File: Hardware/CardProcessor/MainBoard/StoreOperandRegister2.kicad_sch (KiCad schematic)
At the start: 2 parts, among them U43 74ABT16374

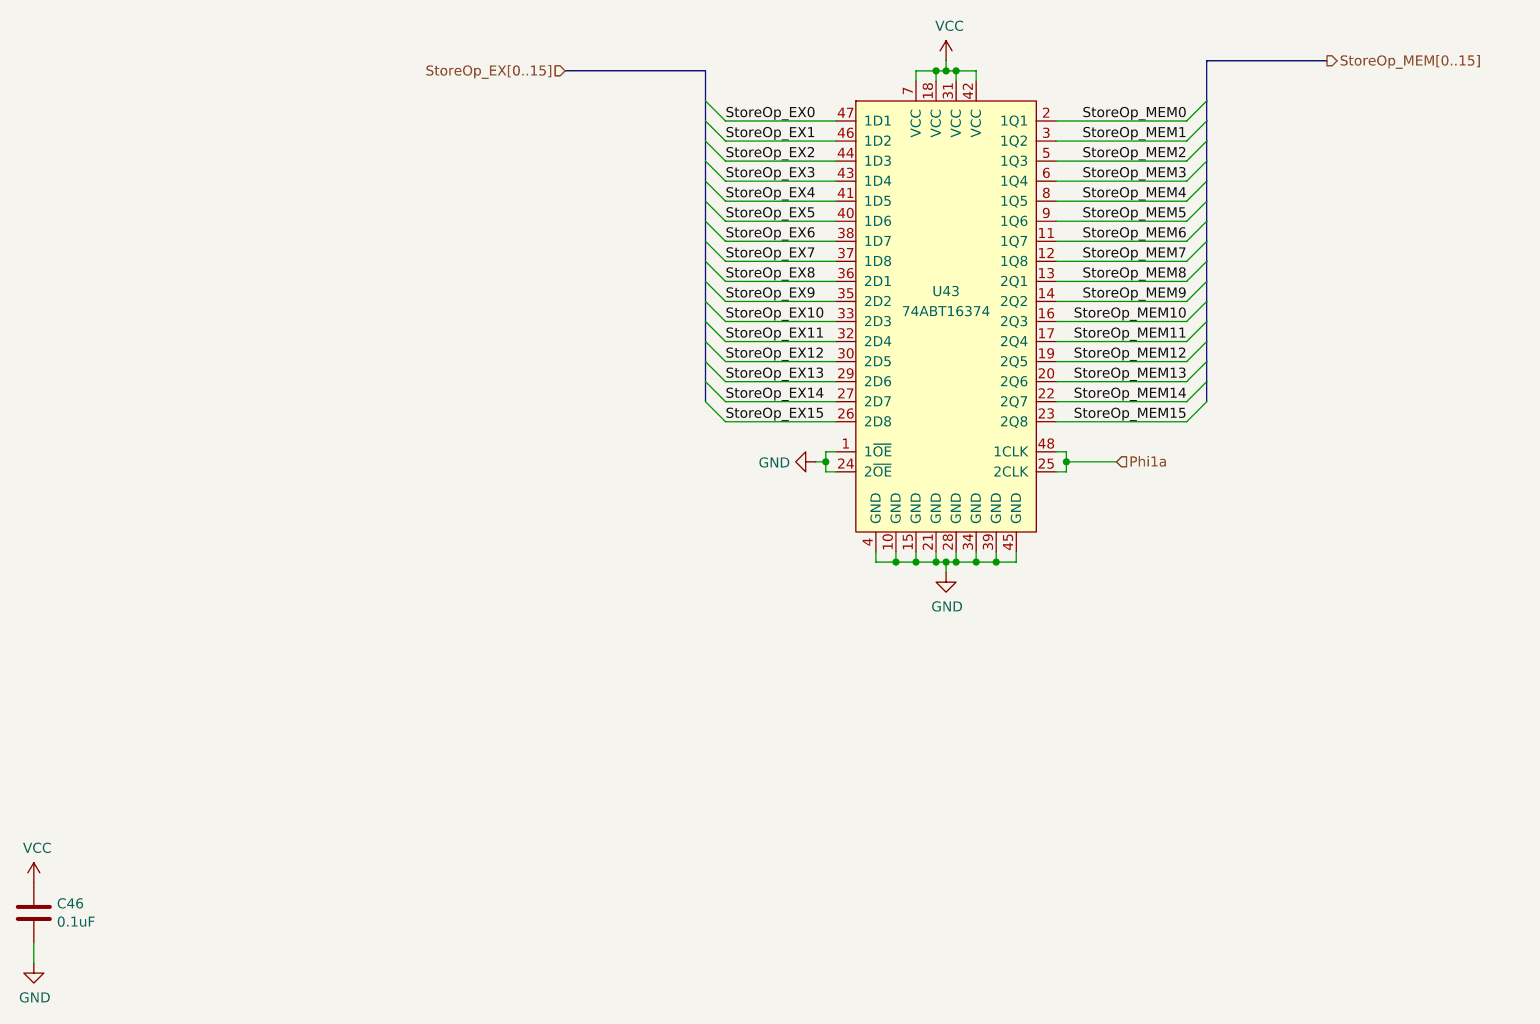
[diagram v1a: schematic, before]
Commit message: Extract EX to new EXModule sheet
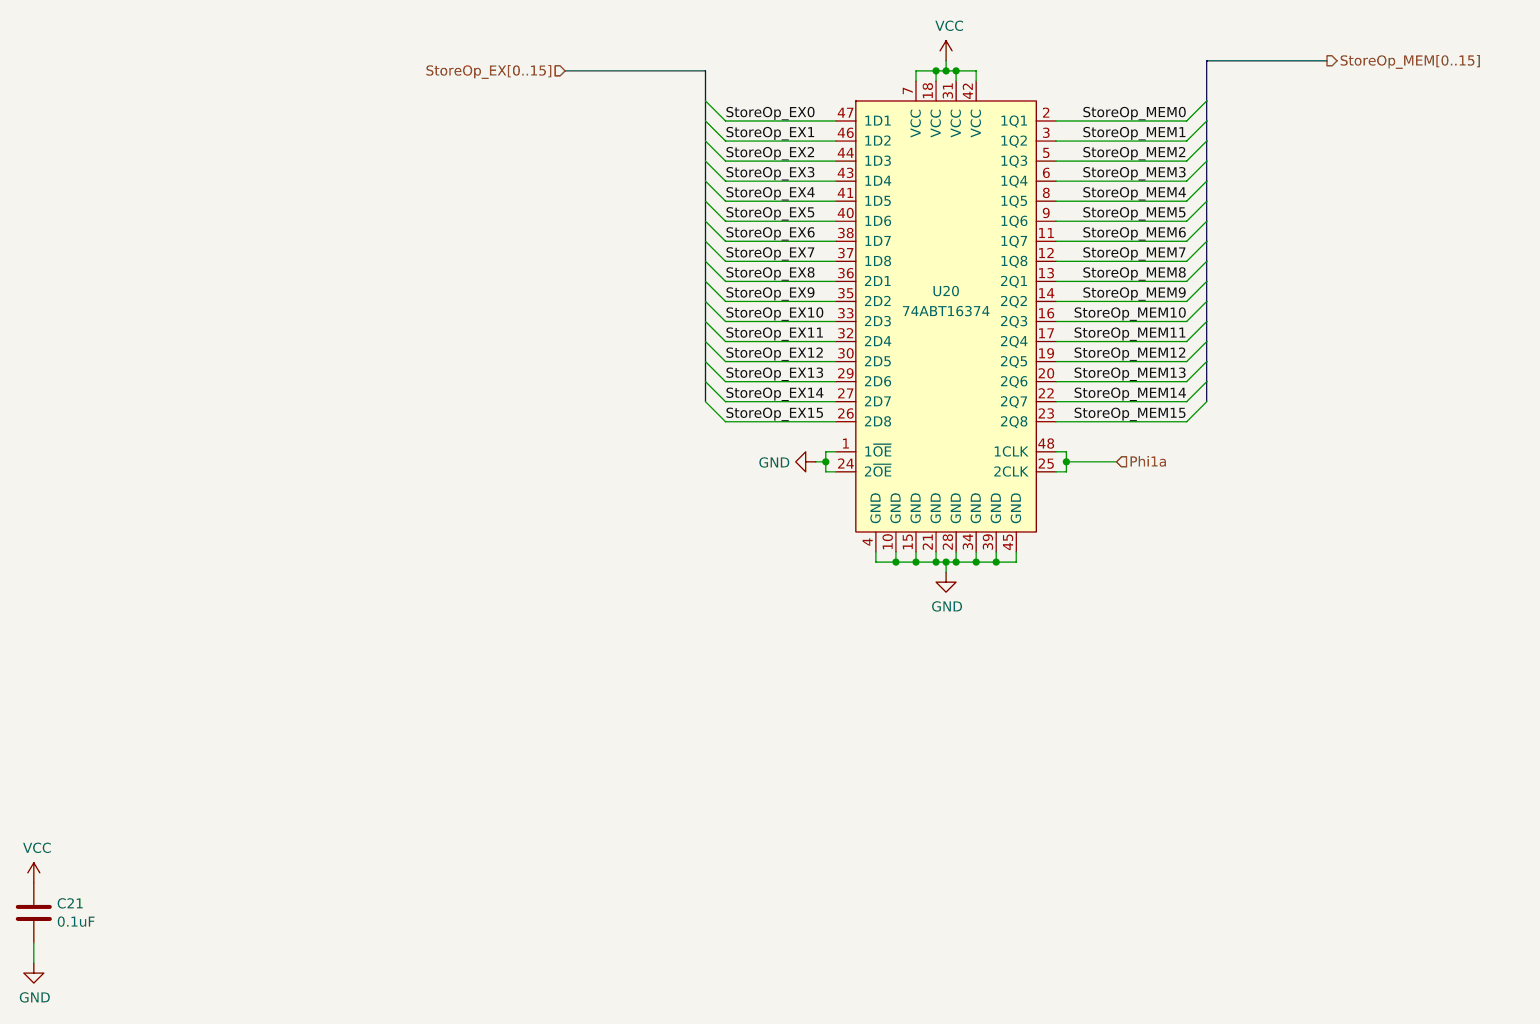
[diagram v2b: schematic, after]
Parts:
- renumbered C46 to C21, U43 to U20
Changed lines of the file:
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@@
 		(on_board yes)
 		(dnp no)
-		(property "Reference" "C46"
+		(property "Reference" "C21"
 			(at 32.131 177.9016 0)
 			(effects
@@
 		(instances
 			(project "MainBoard"
-				(path "/83c5181e-f5ee-453c-ae5c-d7256ba8837d/00000000-0000-0000-0000-000060a71bbf/00000000-0000-0000-0000-00005fd8d6fe"
-					(reference "C46")
+				(path "/83c5181e-f5ee-453c-ae5c-d7256ba8837d/637456a4-4ee5-48ca-bb06-9734ef3462ed/54d68a2e-0685-421b-bbc3-ead3c7c2b0a7/00000000-0000-0000-0000-00005fd8d6fe"
+					(reference "C21")
 					(unit 1)
 				)
@@
 		(on_board yes)
 		(dnp no)
-		(property "Reference" "#PWR0303"
+		(property "Reference" "#PWR0110"
 			(at 29.21 179.07 0)
 			(effects
@@
 		(instances
 			(project "MainBoard"
-				(path "/83c5181e-f5ee-453c-ae5c-d7256ba8837d/00000000-0000-0000-0000-000060a71bbf/00000000-0000-0000-0000-00005fd8d6fe"
-					(reference "#PWR0303")
+				(path "/83c5181e-f5ee-453c-ae5c-d7256ba8837d/637456a4-4ee5-48ca-bb06-9734ef3462ed/54d68a2e-0685-421b-bbc3-ead3c7c2b0a7/00000000-0000-0000-0000-00005fd8d6fe"
+					(reference "#PWR0110")
 					(unit 1)
 				)
@@
 		(on_board yes)
 		(dnp no)
-		(property "Reference" "#PWR0304"
+		(property "Reference" "#PWR0111"
 			(at 29.21 191.77 0)
 			(effects
@@
 		(instances
 			(project "MainBoard"
-				(path "/83c5181e-f5ee-453c-ae5c-d7256ba8837d/00000000-0000-0000-0000-000060a71bbf/00000000-0000-0000-0000-00005fd8d6fe"
-					(reference "#PWR0304")
+				(path "/83c5181e-f5ee-453c-ae5c-d7256ba8837d/637456a4-4ee5-48ca-bb06-9734ef3462ed/54d68a2e-0685-421b-bbc3-ead3c7c2b0a7/00000000-0000-0000-0000-00005fd8d6fe"
+					(reference "#PWR0111")
 					(unit 1)
 				)
@@
 		(on_board yes)
 		(dnp no)
-		(property "Reference" "#PWR0305"
+		(property "Reference" "#PWR0112"
 			(at 121.92 121.92 0)
 			(effects
@@
 		(instances
 			(project "MainBoard"
-				(path "/83c5181e-f5ee-453c-ae5c-d7256ba8837d/00000000-0000-0000-0000-000060a71bbf/00000000-0000-0000-0000-00005fd8d6fe"
-					(reference "#PWR0305")
+				(path "/83c5181e-f5ee-453c-ae5c-d7256ba8837d/637456a4-4ee5-48ca-bb06-9734ef3462ed/54d68a2e-0685-421b-bbc3-ead3c7c2b0a7/00000000-0000-0000-0000-00005fd8d6fe"
+					(reference "#PWR0112")
 					(unit 1)
 				)
@@
 		(on_board yes)
 		(dnp no)
-		(property "Reference" "#PWR0306"
+		(property "Reference" "#PWR0113"
 			(at 144.78 74.93 0)
 			(effects
@@
 		(instances
 			(project "MainBoard"
-				(path "/83c5181e-f5ee-453c-ae5c-d7256ba8837d/00000000-0000-0000-0000-000060a71bbf/00000000-0000-0000-0000-00005fd8d6fe"
-					(reference "#PWR0306")
+				(path "/83c5181e-f5ee-453c-ae5c-d7256ba8837d/637456a4-4ee5-48ca-bb06-9734ef3462ed/54d68a2e-0685-421b-bbc3-ead3c7c2b0a7/00000000-0000-0000-0000-00005fd8d6fe"
+					(reference "#PWR0113")
 					(unit 1)
 				)
@@
 		(on_board yes)
 		(dnp no)
-		(property "Reference" "#PWR0307"
+		(property "Reference" "#PWR0114"
 			(at 144.78 142.24 0)
 			(effects
@@
 		(instances
 			(project "MainBoard"
-				(path "/83c5181e-f5ee-453c-ae5c-d7256ba8837d/00000000-0000-0000-0000-000060a71bbf/00000000-0000-0000-0000-00005fd8d6fe"
-					(reference "#PWR0307")
+				(path "/83c5181e-f5ee-453c-ae5c-d7256ba8837d/637456a4-4ee5-48ca-bb06-9734ef3462ed/54d68a2e-0685-421b-bbc3-ead3c7c2b0a7/00000000-0000-0000-0000-00005fd8d6fe"
+					(reference "#PWR0114")
 					(unit 1)
 				)
@@
 		(on_board yes)
 		(dnp no)
-		(property "Reference" "U43"
+		(property "Reference" "U20"
 			(at 144.78 100.33 0)
 			(effects
@@
 		(instances
 			(project "MainBoard"
-				(path "/83c5181e-f5ee-453c-ae5c-d7256ba8837d/00000000-0000-0000-0000-000060a71bbf/00000000-0000-0000-0000-00005fd8d6fe"
-					(reference "U43")
-					(unit 1)
-				)
+				(path "/83c5181e-f5ee-453c-ae5c-d7256ba8837d/637456a4-4ee5-48ca-bb06-9734ef3462ed/54d68a2e-0685-421b-bbc3-ead3c7c2b0a7/00000000-0000-0000-0000-00005fd8d6fe"
+					(reference "U20")
+					(unit 1)
+				)

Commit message: Reannotate schematic by hand since extracting to new sheets broke existing annotations
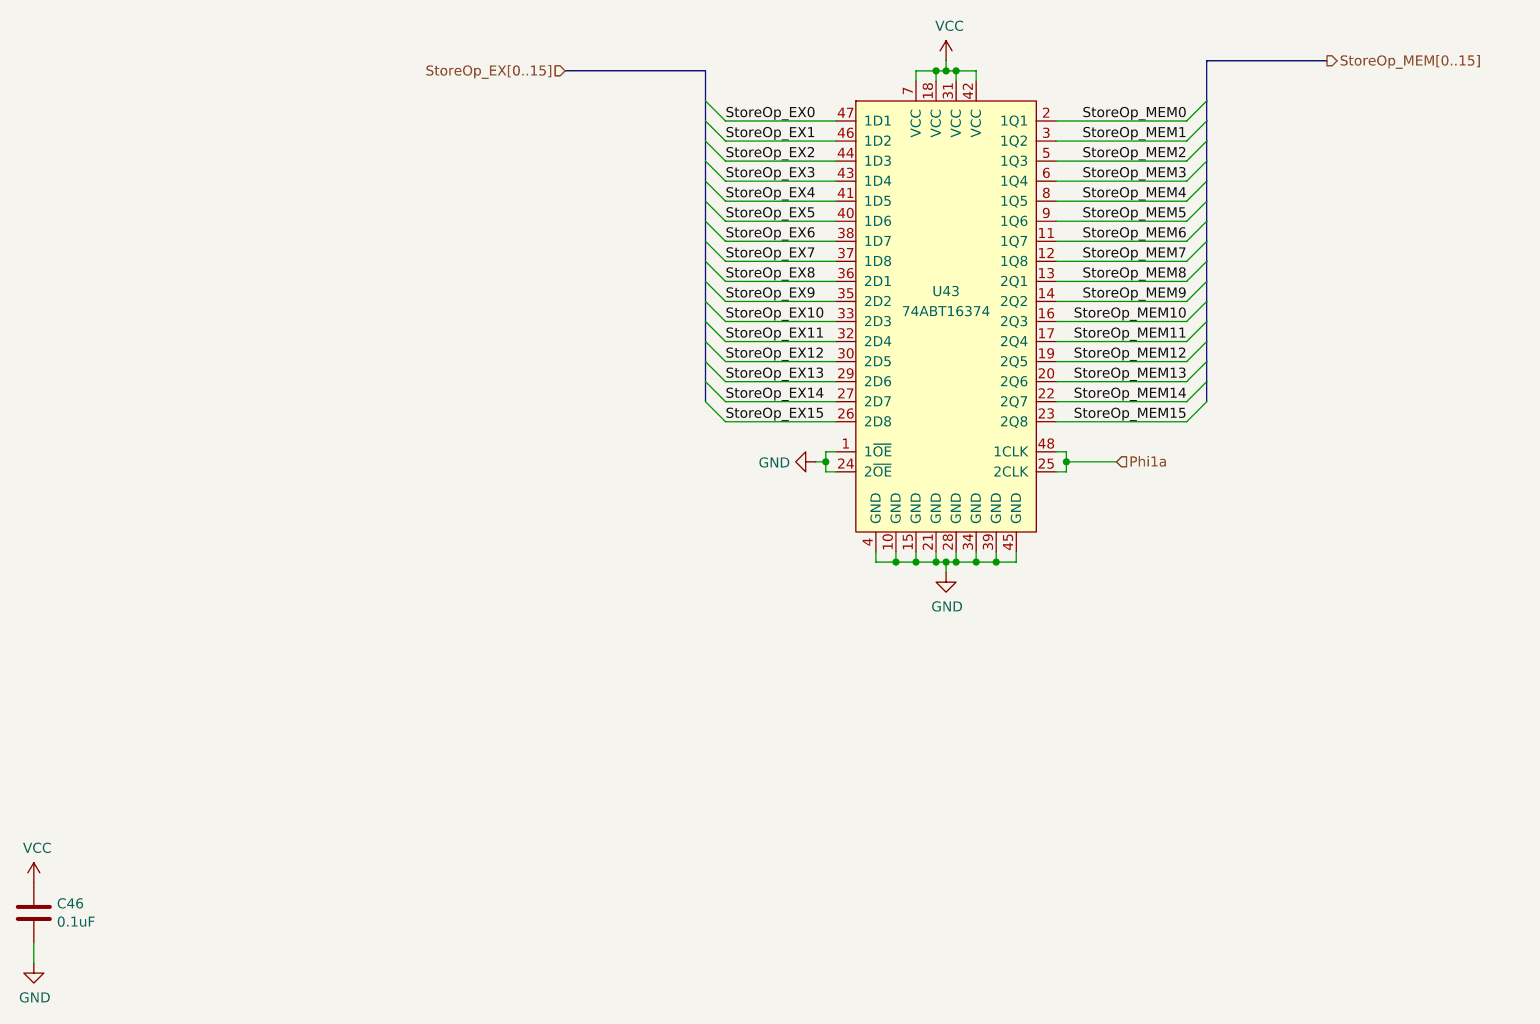
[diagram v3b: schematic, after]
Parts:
- renumbered C21 to C46, U20 to U43
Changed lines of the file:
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@@
 		(on_board yes)
 		(dnp no)
-		(property "Reference" "C21"
+		(property "Reference" "C46"
 			(at 32.131 177.9016 0)
 			(effects
@@
 			(project "MainBoard"
 				(path "/83c5181e-f5ee-453c-ae5c-d7256ba8837d/637456a4-4ee5-48ca-bb06-9734ef3462ed/54d68a2e-0685-421b-bbc3-ead3c7c2b0a7/00000000-0000-0000-0000-00005fd8d6fe"
-					(reference "C21")
+					(reference "C46")
 					(unit 1)
 				)
@@
 		(on_board yes)
 		(dnp no)
-		(property "Reference" "U20"
+		(property "Reference" "U43"
 			(at 144.78 100.33 0)
 			(effects
@@
 			(project "MainBoard"
 				(path "/83c5181e-f5ee-453c-ae5c-d7256ba8837d/637456a4-4ee5-48ca-bb06-9734ef3462ed/54d68a2e-0685-421b-bbc3-ead3c7c2b0a7/00000000-0000-0000-0000-00005fd8d6fe"
-					(reference "U20")
-					(unit 1)
-				)
+					(reference "U43")
+					(unit 1)
+				)
